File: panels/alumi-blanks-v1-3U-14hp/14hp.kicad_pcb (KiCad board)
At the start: 2 copper layers, 70.8 x 128.5 mm, 2 parts

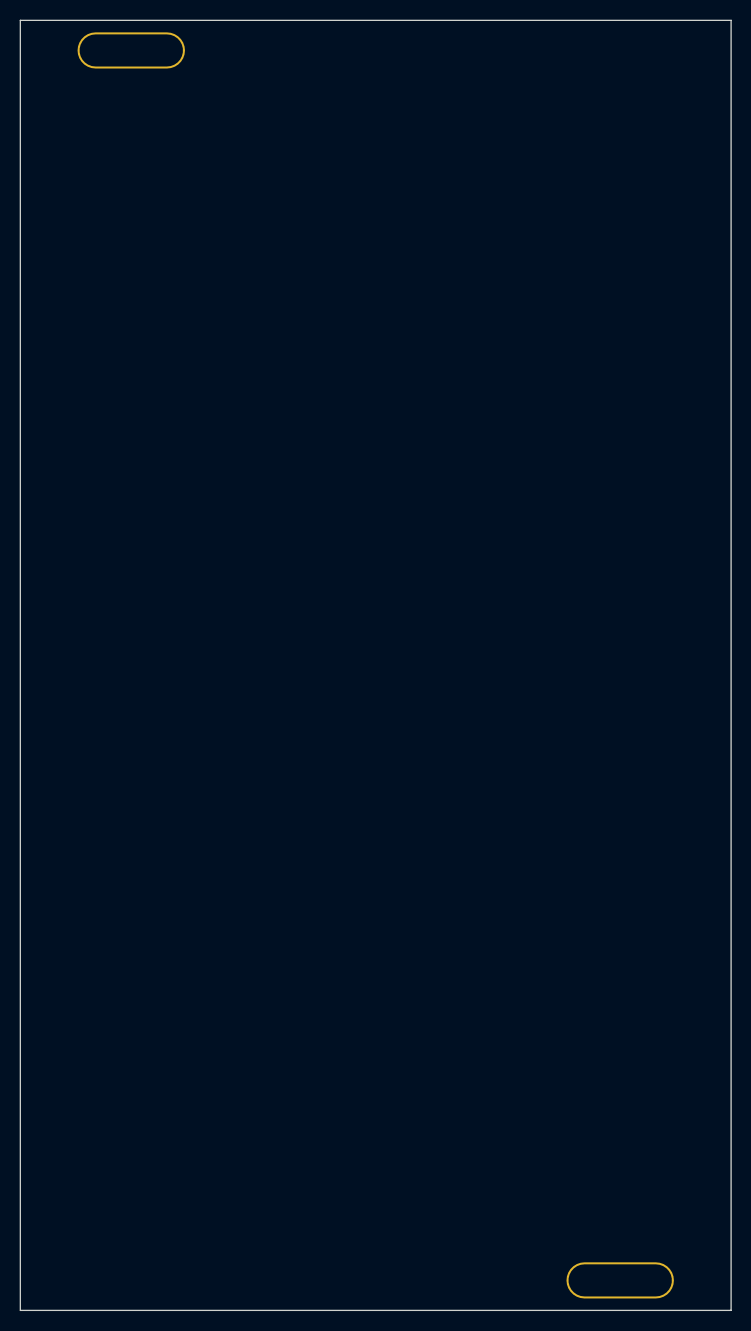
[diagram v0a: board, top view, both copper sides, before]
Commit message: feat: add new screw hole footprints and update panel KiCad files for new JLCPCB order
- Added modular-3M-screw-hole-size1-alumi-0604, modular-3M-screw-hole-size1-fit-alumi-0604, modular-3M-screw-hole-size2-alumi-0604
- Updated all panel .kicad_pcb and .kicad_pro files for 3U panels (1hp-16hp)
- Added new JLCPCB order snapshot and Gerber outputs

Co-authored-by: Copilot <223556219+Copilot@users.noreply.github.com>
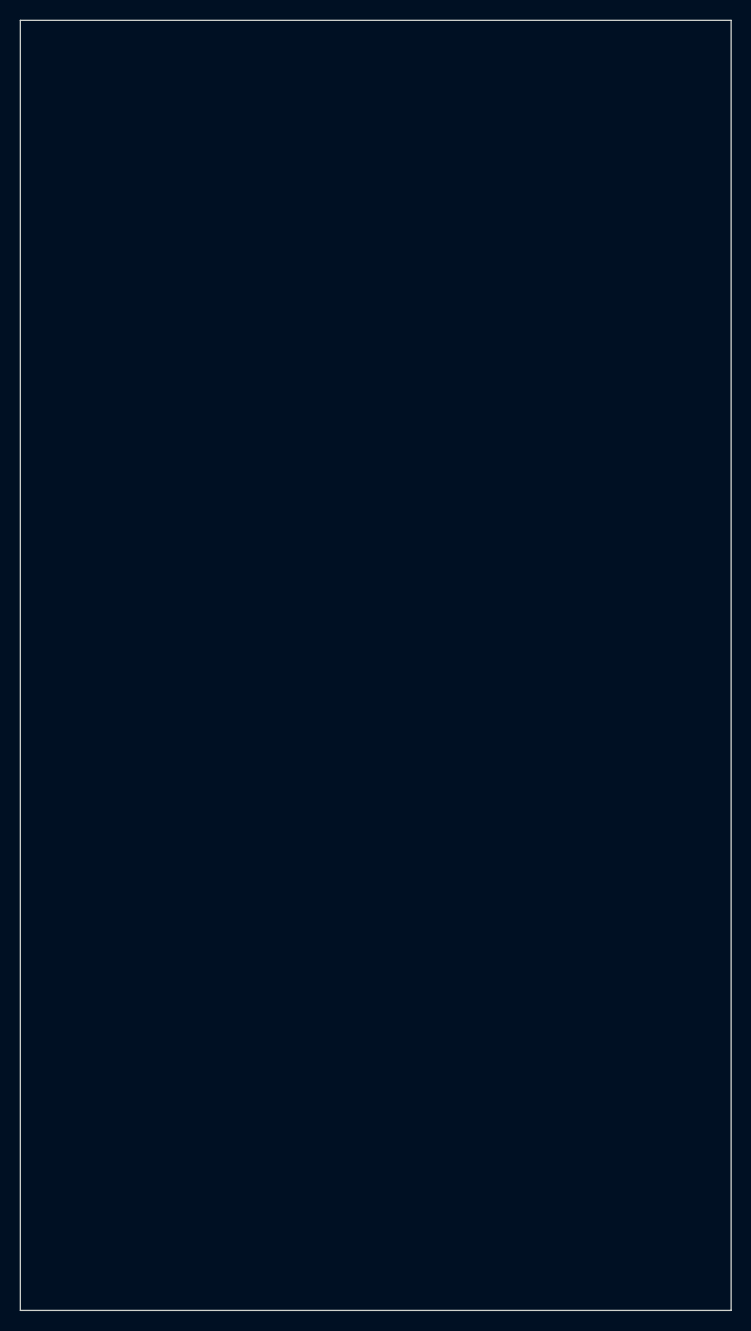
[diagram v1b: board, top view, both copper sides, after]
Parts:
- removed the REF** at (11.1, 3.00)
- removed the REF** at (59.8, 125.5)
- added REF**: modular-3M-screw-hole-size2-alumi-0604, zudo-blanks:modular-3M-screw-hole-size2-alumi-0604, F.Cu at (10.2, 3.00)
- added REF**: modular-3M-screw-hole-size2-alumi-0604, zudo-blanks:modular-3M-screw-hole-size2-alumi-0604, F.Cu at (60.6, 3.00)
- added REF**: modular-3M-screw-hole-size2-alumi-0604, zudo-blanks:modular-3M-screw-hole-size2-alumi-0604, F.Cu at (10.2, 125.5)
- added REF**: modular-3M-screw-hole-size2-alumi-0604, zudo-blanks:modular-3M-screw-hole-size2-alumi-0604, F.Cu at (60.6, 125.5)
